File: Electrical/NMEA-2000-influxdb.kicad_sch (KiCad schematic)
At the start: 4 parts, among them U1 LM7805_TO220

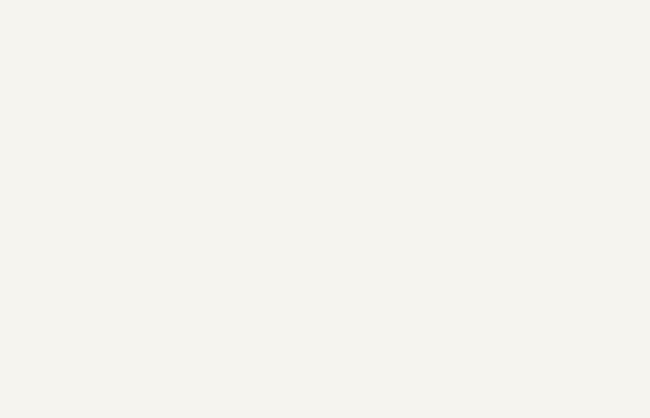
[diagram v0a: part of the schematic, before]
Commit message: Added SN65HVD230 Module to schematic
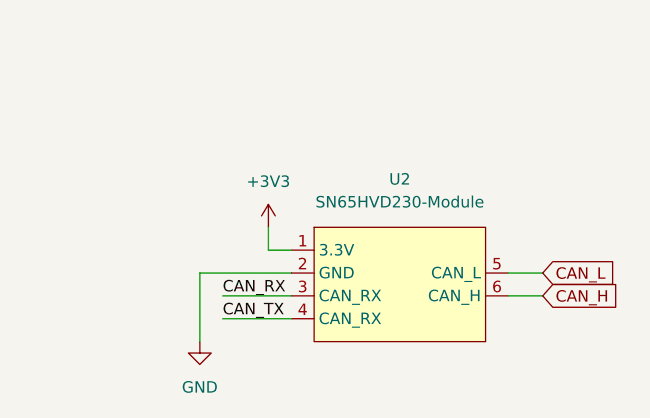
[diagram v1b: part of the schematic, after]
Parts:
- added U2: SN65HVD230-Module, symbol sn65hvd230-module:SN65HVD230-Module
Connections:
- net +3V3: now also U2.1 (3.3V)
- net GND: now also U2.2 (GND)
- new net CAN_H: U2.6 (CAN_H)
- new net CAN_L: U2.5 (CAN_L)
- new net CAN_RX: U2.3 (CAN_RX)
- new net CAN_TX: U2.4 (CAN_RX)
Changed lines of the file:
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@@
   (junction (at 216.154 40.386) (diameter 0) (color 0 0 0 0)
   )
+  (wire (pts (xy 245.11 139.7) (xy 248.92 139.7))
+    (stroke (width 0) (type default))
+  )
   (wire (pts (xy 140.843 73.533) (xy 140.843 76.073))
     (stroke (width 0) (type default))
@@
     (stroke (width 0) (type default))
   )
+  (wire (pts (xy 210.82 137.16) (xy 210.82 144.78))
+    (stroke (width 0) (type default))
+  )
+  (wire (pts (xy 218.44 134.62) (xy 220.98 134.62))
+    (stroke (width 0) (type default))
+  )
   (wire (pts (xy 226.314 50.546) (xy 236.474 50.546))
     (stroke (width 0) (type default))
@@
     (stroke (width 0) (type default))
   )
+  (wire (pts (xy 213.36 139.7) (xy 220.98 139.7))
+    (stroke (width 0) (type default))
+  )
   (wire (pts (xy 233.934 40.386) (xy 236.474 40.386))
     (stroke (width 0) (type default))
@@
     (stroke (width 0) (type default))
   )
+  (wire (pts (xy 245.11 137.16) (xy 248.92 137.16))
+    (stroke (width 0) (type default))
+  )
+  (wire (pts (xy 213.36 142.24) (xy 220.98 142.24))
+    (stroke (width 0) (type default))
+  )
+  (wire (pts (xy 220.98 137.16) (xy 210.82 137.16))
+    (stroke (width 0) (type default))
+  )
+  (wire (pts (xy 218.44 132.08) (xy 218.44 134.62))
+    (stroke (width 0) (type default))
+  )
   (wire (pts (xy 216.154 50.546) (xy 226.314 50.546))
     (stroke (width 0) (type default))
@@
   (wire (pts (xy 216.154 37.846) (xy 216.154 40.386))
     (stroke (width 0) (type default))
+  )
+  (label "CAN_RX" (at 213.36 139.7 0) (fields_autoplaced)
+    (effects (font (size 1.27 1.27)) (justify left bottom))
+  )
+  (label "CAN_TX" (at 213.36 142.24 0) (fields_autoplaced)
+    (effects (font (size 1.27 1.27)) (justify left bottom))
+  )
+  (global_label "CAN_L" (shape input) (at 248.92 137.16 0) (fields_autoplaced)
+    (effects (font (size 1.27 1.27)) (justify left))
+    (property "Intersheetrefs" "${INTERSHEET_REFS}" (at 257.59 137.16 0)
+      (effects (font (size 1.27 1.27)) (justify left) hide)
+    )
+  )
+  (global_label "CAN_H" (shape input) (at 248.92 139.7 0) (fields_autoplaced)
+    (effects (font (size 1.27 1.27)) (justify left))
+    (property "Intersheetrefs" "${INTERSHEET_REFS}" (at 257.8924 139.7 0)
+      (effects (font (size 1.27 1.27)) (justify left) hide)
+    )
   )
   (symbol (lib_id "Device:C_Small") (at 216.154 45.466 0) (unit 1)
@@
     )
   )
+  (symbol (lib_id "power:GND") (at 210.82 144.78 0) (unit 1)
+    (in_bom yes) (on_board yes) (dnp no) (fields_autoplaced)
+    (property "Reference" "#PWR08" (at 210.82 151.13 0)
+      (effects (font (size 1.27 1.27)) hide)
+    )
+    (property "Value" "GND" (at 210.82 149.86 0)
+      (effects (font (size 1.27 1.27)))
+    )
+    (property "Footprint" "" (at 210.82 144.78 0)
+      (effects (font (size 1.27 1.27)) hide)
+    )
+    (property "Datasheet" "" (at 210.82 144.78 0)
+      (effects (font (size 1.27 1.27)) hide)
+    )
+    (pin "1")
+    (instances
+      (project "NMEA-2000-influxdb"
+        (path "/efe7a42c-525a-4afc-8476-4cc785240ca6"
+          (reference "#PWR08") (unit 1)
+        )
+      )
+    )
+  )
   (symbol (lib_id "power:+5V") (at 236.474 37.846 0) (unit 1)
     (in_bom yes) (on_board yes) (dnp no) (fields_autoplaced)
@@
     )
   )
+  (symbol (lib_id "sn65hvd230-module:SN65HVD230-Module") (at 232.41 132.08 0) (unit 1)
+    (in_bom yes) (on_board yes) (dnp no) (fields_autoplaced)
+    (property "Reference" "U2" (at 233.045 126.746 0)
+      (effects (font (size 1.27 1.27)))
+    )
+    (property "Value" "SN65HVD230-Module" (at 233.045 129.286 0)
+      (effects (font (size 1.27 1.27)))
+    )
+    (property "Footprint" "" (at 231.14 132.08 0)
+      (effects (font (size 1.27 1.27)) hide)
+    )
+    (property "Datasheet" "" (at 231.14 132.08 0)
+      (effects (font (size 1.27 1.27)) hide)
+    )
+    (pin "1")
+    (pin "2")
+    (pin "3")
+    (pin "4")
+    (pin "5")
+    (pin "6")
+    (instances
+      (project "NMEA-2000-influxdb"
+        (path "/efe7a42c-525a-4afc-8476-4cc785240ca6"
+          (reference "U2") (unit 1)
+        )
+      )
+    )
+  )
   (symbol (lib_id "power:+12V") (at 216.154 37.846 0) (unit 1)
     (in_bom yes) (on_board yes) (dnp no) (fields_autoplaced)
@@
         )
       )
+    )
+  )
+  (symbol (lib_id "power:+3V3") (at 218.44 132.08 0) (unit 1)
+    (in_bom yes) (on_board yes) (dnp no) (fields_autoplaced)
+    (property "Reference" "#PWR07" (at 218.44 135.89 0)
+      (effects (font (size 1.27 1.27)) hide)
+    )
+    (property "Value" "+3V3" (at 218.44 127 0)
+      (effects (font (size 1.27 1.27)))
+    )
+    (property "Footprint" "" (at 218.44 132.08 0)
+      (effects (font (size 1.27 1.27)) hide)
+    )
+    (property "Datasheet" "" (at 218.44 132.08 0)
+      (effects (font (size 1.27 1.27)) hide)
+    )
+    (pin "1")
+    (instances
+      (project "NMEA-2000-influxdb"
+        (path "/efe7a42c-525a-4afc-8476-4cc785240ca6"
+          (reference "#PWR07") (unit 1)
+        )
+      )

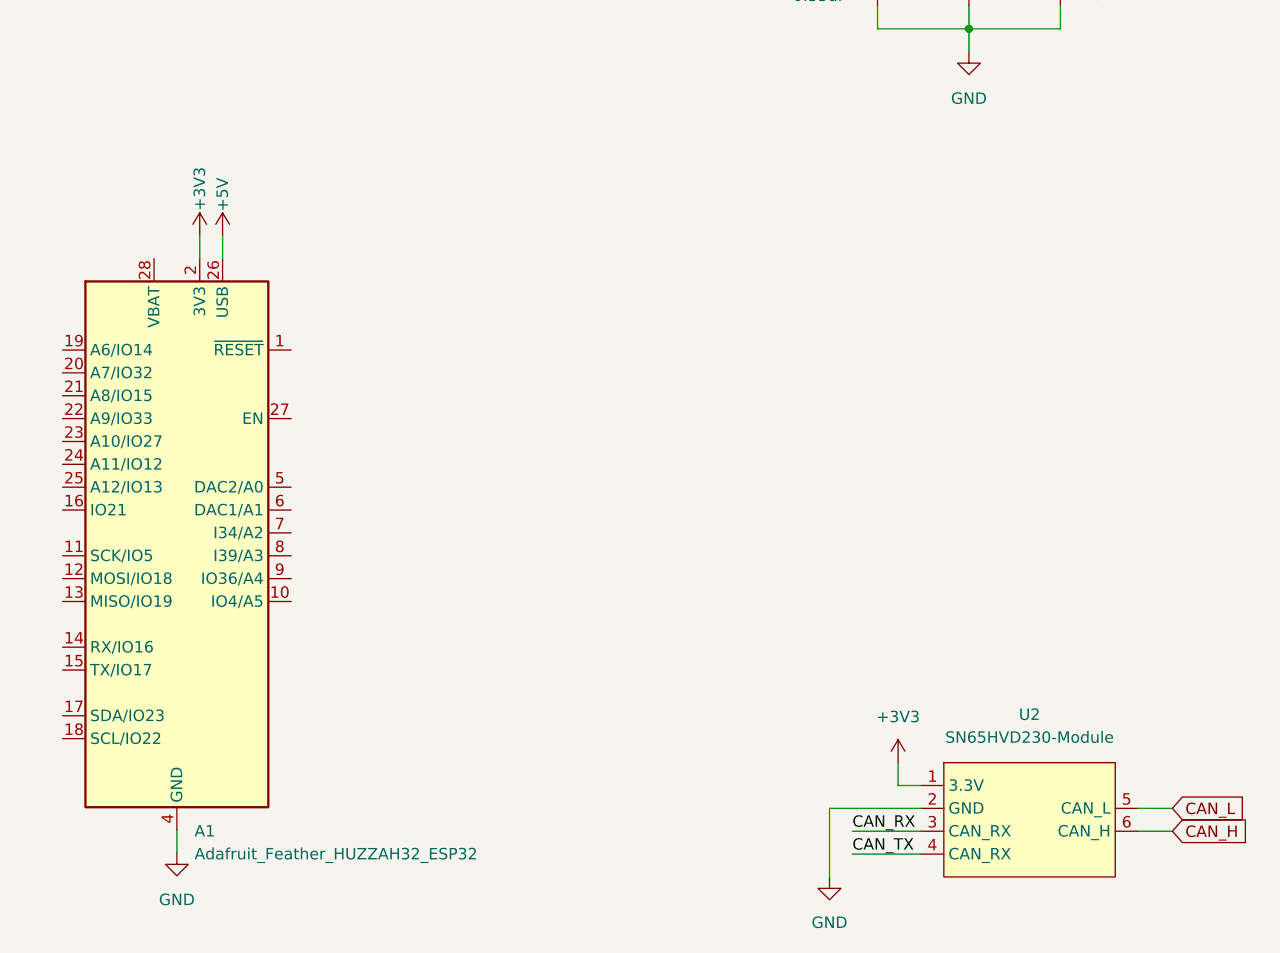
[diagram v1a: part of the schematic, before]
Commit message: Added RTC-Module to schematic
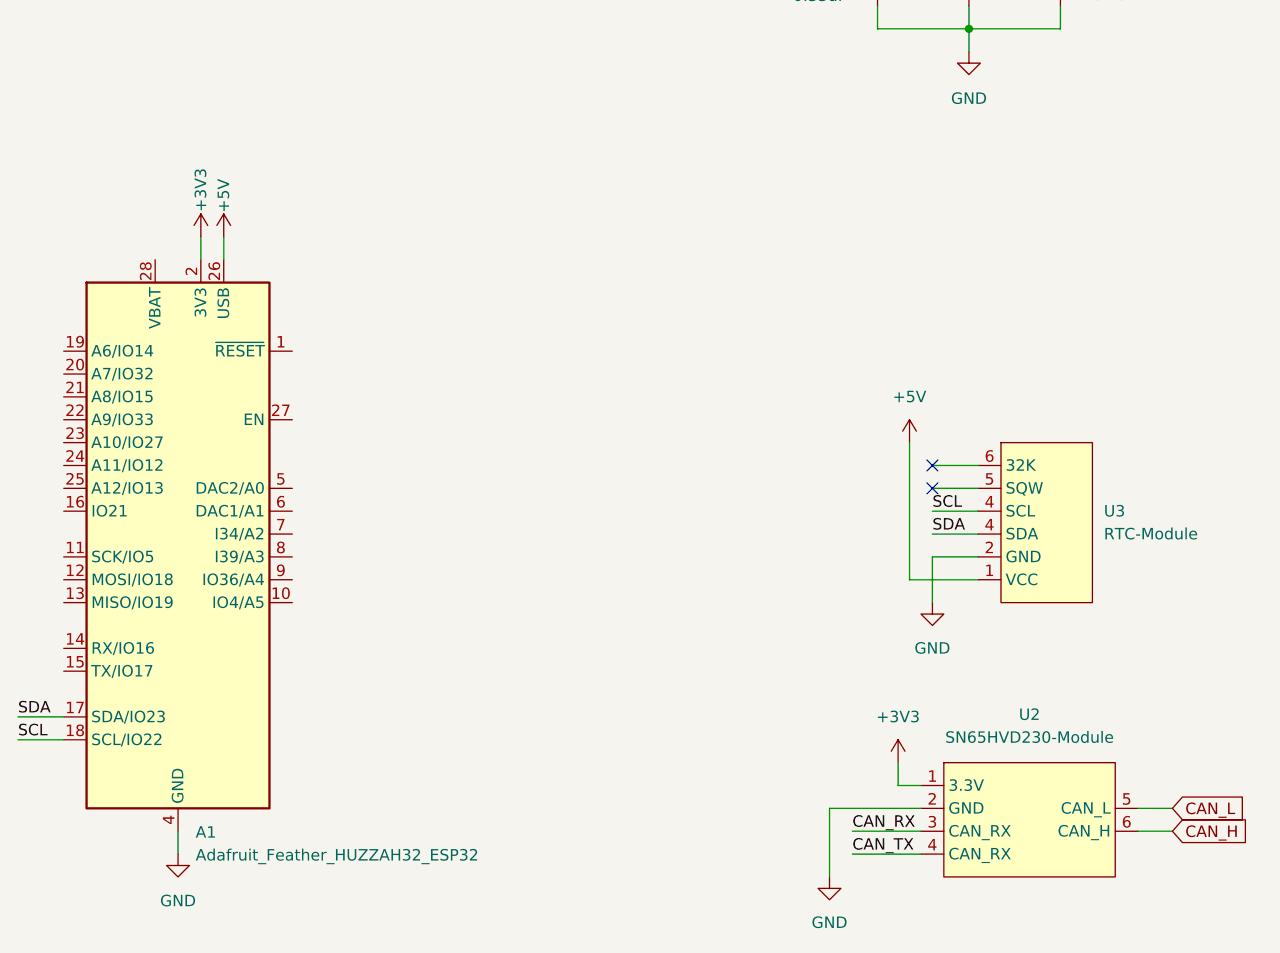
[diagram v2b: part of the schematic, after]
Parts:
- added U3: RTC-Module, symbol RTC-Module:RTC-Module
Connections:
- net +5V: now also U3.1 (VCC)
- net GND: now also U3.2 (GND)
- net SDA: now reaches A1.17 (SDA/IO23)
- net SDA: now also U3.4 (SDA)
- net SCL: now reaches A1.18 (SCL/IO22)
- net SCL: now also U3.4 (SDA)
- no-connect marks 0 -> 2
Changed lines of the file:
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@@
   (junction (at 216.154 40.386) (diameter 0) (color 0 0 0 0)
   )
+  (no_connect (at 222.25 99.06))
+  (no_connect (at 222.25 101.6))
+  (wire (pts (xy 222.25 99.06) (xy 227.33 99.06))
+    (stroke (width 0) (type default))
+  )
+  (wire (pts (xy 222.25 109.22) (xy 222.25 114.3))
+    (stroke (width 0) (type default))
+  )
   (wire (pts (xy 245.11 139.7) (xy 248.92 139.7))
     (stroke (width 0) (type default))
   )
-  (wire (pts (xy 140.843 73.533) (xy 140.843 76.073))
-    (stroke (width 0) (type default))
-  )
-  (wire (pts (xy 143.383 73.533) (xy 143.383 76.073))
+  (wire (pts (xy 140.97 73.66) (xy 140.97 76.2))
+    (stroke (width 0) (type default))
+  )
+  (wire (pts (xy 143.51 73.66) (xy 143.51 76.2))
     (stroke (width 0) (type default))
   )
@@
     (stroke (width 0) (type default))
   )
+  (wire (pts (xy 120.65 127) (xy 125.73 127))
+    (stroke (width 0) (type default))
+  )
   (wire (pts (xy 236.474 40.386) (xy 236.474 42.926))
     (stroke (width 0) (type default))
   )
-  (wire (pts (xy 138.303 139.573) (xy 138.303 142.113))
+  (wire (pts (xy 120.65 129.54) (xy 125.73 129.54))
+    (stroke (width 0) (type default))
+  )
+  (wire (pts (xy 222.25 101.6) (xy 227.33 101.6))
+    (stroke (width 0) (type default))
+  )
+  (wire (pts (xy 138.43 139.7) (xy 138.43 142.24))
+    (stroke (width 0) (type default))
+  )
+  (wire (pts (xy 222.25 106.68) (xy 227.33 106.68))
+    (stroke (width 0) (type default))
+  )
+  (wire (pts (xy 222.25 104.14) (xy 227.33 104.14))
+    (stroke (width 0) (type default))
+  )
+  (wire (pts (xy 219.71 96.52) (xy 219.71 111.76))
     (stroke (width 0) (type default))
   )
@@
     (stroke (width 0) (type default))
   )
+  (wire (pts (xy 227.33 111.76) (xy 219.71 111.76))
+    (stroke (width 0) (type default))
+  )
+  (wire (pts (xy 227.33 109.22) (xy 222.25 109.22))
+    (stroke (width 0) (type default))
+  )
+  (label "SCL" (at 120.65 129.54 0) (fields_autoplaced)
+    (effects (font (size 1.27 1.27)) (justify left bottom))
+  )
   (label "CAN_RX" (at 213.36 139.7 0) (fields_autoplaced)
+    (effects (font (size 1.27 1.27)) (justify left bottom))
+  )
+  (label "SCL" (at 222.25 104.14 0) (fields_autoplaced)
+    (effects (font (size 1.27 1.27)) (justify left bottom))
+  )
+  (label "SDA" (at 120.65 127 0) (fields_autoplaced)
+    (effects (font (size 1.27 1.27)) (justify left bottom))
+  )
+  (label "SDA" (at 222.25 106.68 0) (fields_autoplaced)
     (effects (font (size 1.27 1.27)) (justify left bottom))
   )
@@
     )
   )
-  (symbol (lib_id "power:+3V3") (at 140.843 73.533 0) (unit 1)
+  (symbol (lib_id "power:+3V3") (at 140.97 73.66 0) (unit 1)
     (in_bom yes) (on_board yes) (dnp no)
-    (property "Reference" "#PWR02" (at 140.843 77.343 0)
-      (effects (font (size 1.27 1.27)) hide)
-    )
-    (property "Value" "+3V3" (at 140.843 68.326 90)
-      (effects (font (size 1.27 1.27)))
-    )
-    (property "Footprint" "" (at 140.843 73.533 0)
-      (effects (font (size 1.27 1.27)) hide)
-    )
-    (property "Datasheet" "" (at 140.843 73.533 0)
+    (property "Reference" "#PWR02" (at 140.97 77.47 0)
+      (effects (font (size 1.27 1.27)) hide)
+    )
+    (property "Value" "+3V3" (at 140.97 68.453 90)
+      (effects (font (size 1.27 1.27)))
+    )
+    (property "Footprint" "" (at 140.97 73.66 0)
+      (effects (font (size 1.27 1.27)) hide)
+    )
+    (property "Datasheet" "" (at 140.97 73.66 0)
       (effects (font (size 1.27 1.27)) hide)
     )
@@
         (path "/efe7a42c-525a-4afc-8476-4cc785240ca6"
           (reference "#PWR08") (unit 1)
+        )
+      )
+    )
+  )
+  (symbol (lib_id "RTC-Module:RTC-Module") (at 234.95 96.52 0) (unit 1)
+    (in_bom yes) (on_board yes) (dnp no) (fields_autoplaced)
+    (property "Reference" "U3" (at 241.3 104.14 0)
+      (effects (font (size 1.27 1.27)) (justify left))
+    )
+    (property "Value" "RTC-Module" (at 241.3 106.68 0)
+      (effects (font (size 1.27 1.27)) (justify left))
+    )
+    (property "Footprint" "" (at 234.95 96.52 0)
+      (effects (font (size 1.27 1.27)) hide)
+    )
+    (property "Datasheet" "" (at 234.95 96.52 0)
+      (effects (font (size 1.27 1.27)) hide)
+    )
+    (pin "1")
+    (pin "2")
+    (pin "4")
+    (pin "4")
+    (pin "5")
+    (pin "6")
+    (instances
+      (project "NMEA-2000-influxdb"
+        (path "/efe7a42c-525a-4afc-8476-4cc785240ca6"
+          (reference "U3") (unit 1)
         )
       )
@@
     )
   )
-  (symbol (lib_id "power:GND") (at 138.303 142.113 0) (unit 1)
-    (in_bom yes) (on_board yes) (dnp no) (fields_autoplaced)
-    (property "Reference" "#PWR01" (at 138.303 148.463 0)
-      (effects (font (size 1.27 1.27)) hide)
-    )
-    (property "Value" "GND" (at 138.303 147.32 0)
-      (effects (font (size 1.27 1.27)))
-    )
-    (property "Footprint" "" (at 138.303 142.113 0)
-      (effects (font (size 1.27 1.27)) hide)
-    )
-    (property "Datasheet" "" (at 138.303 142.113 0)
+  (symbol (lib_id "power:+5V") (at 219.71 96.52 0) (unit 1)
+    (in_bom yes) (on_board yes) (dnp no) (fields_autoplaced)
+    (property "Reference" "#PWR010" (at 219.71 100.33 0)
+      (effects (font (size 1.27 1.27)) hide)
+    )
+    (property "Value" "+5V" (at 219.71 91.44 0)
+      (effects (font (size 1.27 1.27)))
+    )
+    (property "Footprint" "" (at 219.71 96.52 0)
+      (effects (font (size 1.27 1.27)) hide)
+    )
+    (property "Datasheet" "" (at 219.71 96.52 0)
+      (effects (font (size 1.27 1.27)) hide)
+    )
+    (pin "1")
+    (instances
+      (project "NMEA-2000-influxdb"
+        (path "/efe7a42c-525a-4afc-8476-4cc785240ca6"
+          (reference "#PWR010") (unit 1)
+        )
+      )
+    )
+  )
+  (symbol (lib_id "power:GND") (at 138.43 142.24 0) (unit 1)
+    (in_bom yes) (on_board yes) (dnp no) (fields_autoplaced)
+    (property "Reference" "#PWR01" (at 138.43 148.59 0)
+      (effects (font (size 1.27 1.27)) hide)
+    )
+    (property "Value" "GND" (at 138.43 147.447 0)
+      (effects (font (size 1.27 1.27)))
+    )
+    (property "Footprint" "" (at 138.43 142.24 0)
+      (effects (font (size 1.27 1.27)) hide)
+    )
+    (property "Datasheet" "" (at 138.43 142.24 0)
       (effects (font (size 1.27 1.27)) hide)
     )
@@
     )
   )
-  (symbol (lib_id "MCU_Module:Adafruit_Feather_HUZZAH32_ESP32") (at 138.303 106.553 0) (unit 1)
-    (in_bom yes) (on_board yes) (dnp no) (fields_autoplaced)
-    (property "Reference" "A1" (at 140.2589 139.7 0)
-      (effects (font (size 1.27 1.27)) (justify left))
-    )
-    (property "Value" "Adafruit_Feather_HUZZAH32_ESP32" (at 140.2589 142.24 0)
-      (effects (font (size 1.27 1.27)) (justify left))
-    )
-    (property "Footprint" "Module:Adafruit_Feather" (at 140.843 140.843 0)
+  (symbol (lib_id "MCU_Module:Adafruit_Feather_HUZZAH32_ESP32") (at 138.43 106.68 0) (unit 1)
+    (in_bom yes) (on_board yes) (dnp no) (fields_autoplaced)
+    (property "Reference" "A1" (at 140.3859 139.827 0)
+      (effects (font (size 1.27 1.27)) (justify left))
+    )
+    (property "Value" "Adafruit_Feather_HUZZAH32_ESP32" (at 140.3859 142.367 0)
+      (effects (font (size 1.27 1.27)) (justify left))
+    )
+    (property "Footprint" "Module:Adafruit_Feather" (at 140.97 140.97 0)
       (effects (font (size 1.27 1.27)) (justify left) hide)
     )
-    (property "Datasheet" "https://cdn-learn.adafruit.com/downloads/pdf/adafruit-huzzah32-esp32-feather.pdf" (at 138.303 137.033 0)
+    (property "Datasheet" "https://cdn-learn.adafruit.com/downloads/pdf/adafruit-huzzah32-esp32-feather.pdf" (at 138.43 137.16 0)
       (effects (font (size 1.27 1.27)) hide)
     )
@@
     )
   )
-  (symbol (lib_id "power:+5V") (at 143.383 73.533 0) (unit 1)
+  (symbol (lib_id "power:+5V") (at 143.51 73.66 0) (unit 1)
     (in_bom yes) (on_board yes) (dnp no)
-    (property "Reference" "#PWR03" (at 143.383 77.343 0)
-      (effects (font (size 1.27 1.27)) hide)
-    )
-    (property "Value" "+5V" (at 143.383 68.961 90)
-      (effects (font (size 1.27 1.27)))
-    )
-    (property "Footprint" "" (at 143.383 73.533 0)
-      (effects (font (size 1.27 1.27)) hide)
-    )
-    (property "Datasheet" "" (at 143.383 73.533 0)
+    (property "Reference" "#PWR03" (at 143.51 77.47 0)
+      (effects (font (size 1.27 1.27)) hide)
+    )
+    (property "Value" "+5V" (at 143.51 69.088 90)
+      (effects (font (size 1.27 1.27)))
+    )
+    (property "Footprint" "" (at 143.51 73.66 0)
+      (effects (font (size 1.27 1.27)) hide)
+    )
+    (property "Datasheet" "" (at 143.51 73.66 0)
       (effects (font (size 1.27 1.27)) hide)
     )
@@
         )
       )
+    )
+  )
+  (symbol (lib_id "power:GND") (at 222.25 114.3 0) (unit 1)
+    (in_bom yes) (on_board yes) (dnp no) (fields_autoplaced)
+    (property "Reference" "#PWR09" (at 222.25 120.65 0)
+      (effects (font (size 1.27 1.27)) hide)
+    )
+    (property "Value" "GND" (at 222.25 119.38 0)
+      (effects (font (size 1.27 1.27)))
+    )
+    (property "Footprint" "" (at 222.25 114.3 0)
+      (effects (font (size 1.27 1.27)) hide)
+    )
+    (property "Datasheet" "" (at 222.25 114.3 0)
+      (effects (font (size 1.27 1.27)) hide)
+    )
+    (pin "1")
+    (instances
+      (project "NMEA-2000-influxdb"
+        (path "/efe7a42c-525a-4afc-8476-4cc785240ca6"
+          (reference "#PWR09") (unit 1)
+        )
+      )
